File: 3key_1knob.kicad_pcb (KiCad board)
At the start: 2 copper layers, 99.2 x 35 mm, 18 parts, among them J1 Conn_01x02, SW1 RotaryEncoder_Switch, U4 Kailh_socket_MX, U5 Kailh_socket_MX, U6 Kailh_socket_MX

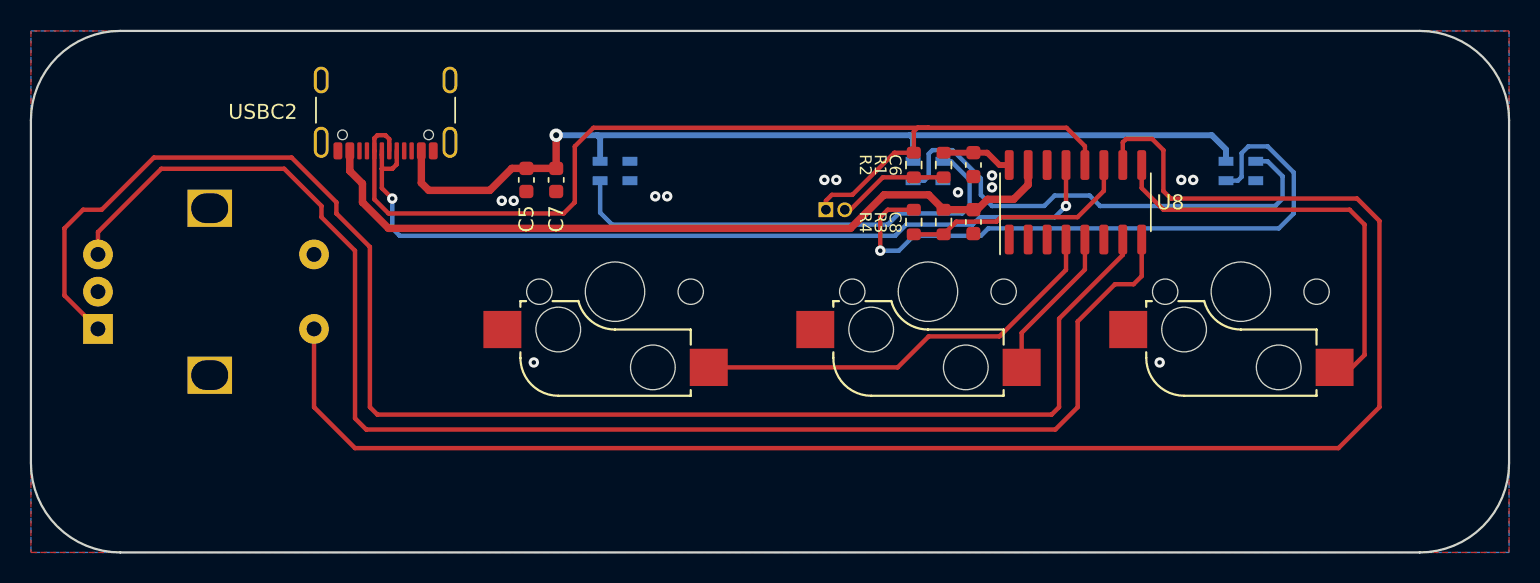
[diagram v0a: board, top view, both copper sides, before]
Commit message: Add mounting holes around corners
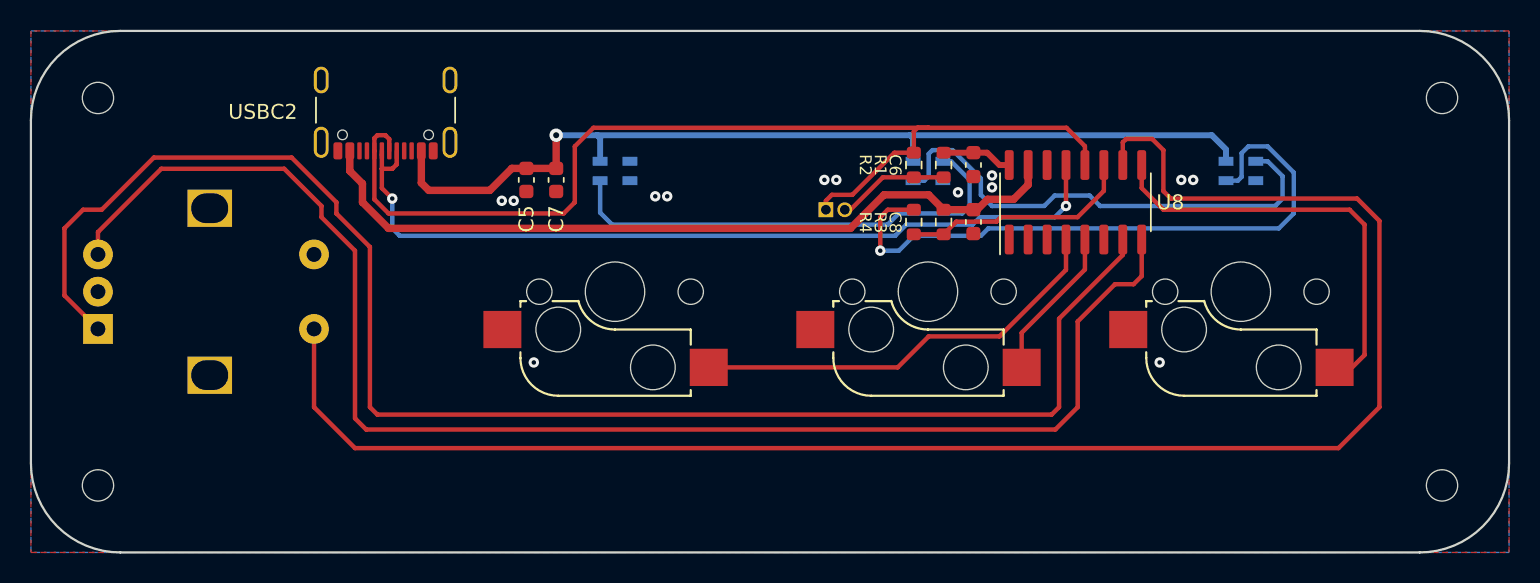
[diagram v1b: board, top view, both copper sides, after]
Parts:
- added REF**: MountingHole_2.1mm, MountingHole:MountingHole_2.1mm, F.Cu at (194.7, 130.5)
- added REF**: MountingHole_2.1mm, MountingHole:MountingHole_2.1mm, F.Cu at (194.7, 104.5)
- added REF**: MountingHole_2.1mm, MountingHole:MountingHole_2.1mm, F.Cu at (104.5, 104.5)
- added REF**: MountingHole_2.1mm, MountingHole:MountingHole_2.1mm, F.Cu at (104.5, 130.5)
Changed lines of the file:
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@@
     )
+  )
+  (footprint "MountingHole:MountingHole_2.1mm" (layer "F.Cu")
+    (at 194.7 130.5)
+    (descr "Mounting Hole 2.1mm, no annular")
+    (tags "mounting hole 2.1mm no annular")
+    (attr exclude_from_pos_files exclude_from_bom)
+    (fp_text reference "REF**" (at 0 -3.2) (layer "F.SilkS") hide
+        (effects (font (size 1 1) (thickness 0.15)))
+    )
+    (fp_text value "MountingHole_2.1mm" (at 0 3.2) (layer "F.Fab") hide
+        (effects (font (size 1 1) (thickness 0.15)))
+    )
+    (fp_text user "${REFERENCE}" (at 0 0) (layer "F.Fab") hide
+        (effects (font (size 1 1) (thickness 0.15)))
+    )
+    (fp_circle (center 0 0) (end 2.1 0)
+      (stroke (width 0.15) (type solid)) (fill none) (layer "Cmts.User"))
+    (fp_circle (center 0 0) (end 2.35 0)
+      (stroke (width 0.05) (type solid)) (fill none) (layer "F.CrtYd"))
+    (pad "" np_thru_hole circle (at 0 0) (size 2.1 2.1) (drill 2.1) (layers "F&B.Cu" "*.Mask"))
   )
   (footprint "Resistor_SMD:R_0603_1608Metric" (layer "F.Cu")
@@
     )
   )
+  (footprint "MountingHole:MountingHole_2.1mm" (layer "F.Cu")
+    (at 194.7 104.5)
+    (descr "Mounting Hole 2.1mm, no annular")
+    (tags "mounting hole 2.1mm no annular")
+    (attr exclude_from_pos_files exclude_from_bom)
+    (fp_text reference "REF**" (at 0 -3.2) (layer "F.SilkS") hide
+        (effects (font (size 1 1) (thickness 0.15)))
+    )
+    (fp_text value "MountingHole_2.1mm" (at 0 3.2) (layer "F.Fab") hide
+        (effects (font (size 1 1) (thickness 0.15)))
+    )
+    (fp_text user "${REFERENCE}" (at 0 0) (layer "F.Fab") hide
+        (effects (font (size 1 1) (thickness 0.15)))
+    )
+    (fp_circle (center 0 0) (end 2.1 0)
+      (stroke (width 0.15) (type solid)) (fill none) (layer "Cmts.User"))
+    (fp_circle (center 0 0) (end 2.35 0)
+      (stroke (width 0.05) (type solid)) (fill none) (layer "F.CrtYd"))
+    (pad "" np_thru_hole circle (at 0 0) (size 2.1 2.1) (drill 2.1) (layers "F&B.Cu" "*.Mask"))
+  )
   (footprint "Capacitor_SMD:C_0603_1608Metric" (layer "F.Cu")
     (at 163.25 112.825 -90)
@@
       (rotate (xyz 0 0 0))
     )
+  )
+  (footprint "MountingHole:MountingHole_2.1mm" (layer "F.Cu")
+    (at 104.5 104.5)
+    (descr "Mounting Hole 2.1mm, no annular")
+    (tags "mounting hole 2.1mm no annular")
+    (attr exclude_from_pos_files exclude_from_bom)
+    (fp_text reference "REF**" (at 0 -3.2) (layer "F.SilkS") hide
+        (effects (font (size 1 1) (thickness 0.15)))
+    )
+    (fp_text value "MountingHole_2.1mm" (at 0 3.2) (layer "F.Fab") hide
+        (effects (font (size 1 1) (thickness 0.15)))
+    )
+    (fp_text user "${REFERENCE}" (at 0 0) (layer "F.Fab") hide
+        (effects (font (size 1 1) (thickness 0.15)))
+    )
+    (fp_circle (center 0 0) (end 2.1 0)
+      (stroke (width 0.15) (type solid)) (fill none) (layer "Cmts.User"))
+    (fp_circle (center 0 0) (end 2.35 0)
+      (stroke (width 0.05) (type solid)) (fill none) (layer "F.CrtYd"))
+    (pad "" np_thru_hole circle (at 0 0) (size 2.1 2.1) (drill 2.1) (layers "*.Cu" "*.Mask"))
   )
   (footprint "Capacitor_SMD:C_0603_1608Metric" (layer "F.Cu")
@@
     )
   )
+  (footprint "MountingHole:MountingHole_2.1mm" (layer "F.Cu")
+    (at 104.5 130.5)
+    (descr "Mounting Hole 2.1mm, no annular")
+    (tags "mounting hole 2.1mm no annular")
+    (attr exclude_from_pos_files exclude_from_bom)
+    (fp_text reference "REF**" (at 0 -3.2) (layer "F.SilkS") hide
+        (effects (font (size 1 1) (thickness 0.15)))
+    )
+    (fp_text value "MountingHole_2.1mm" (at 0 3.2) (layer "F.Fab") hide
+        (effects (font (size 1 1) (thickness 0.15)))
+    )
+    (fp_text user "${REFERENCE}" (at 0 0) (layer "F.Fab") hide
+        (effects (font (size 1 1) (thickness 0.15)))
+    )
+    (fp_circle (center 0 0) (end 2.1 0)
+      (stroke (width 0.15) (type solid)) (fill none) (layer "Cmts.User"))
+    (fp_circle (center 0 0) (end 2.35 0)
+      (stroke (width 0.05) (type solid)) (fill none) (layer "F.CrtYd"))
+    (pad "" np_thru_hole circle (at 0 0) (size 2.1 2.1) (drill 2.1) (layers "F&B.Cu" "*.Mask"))
+  )
   (footprint "keyswitches:Kailh_socket_MX" (layer "B.Cu")

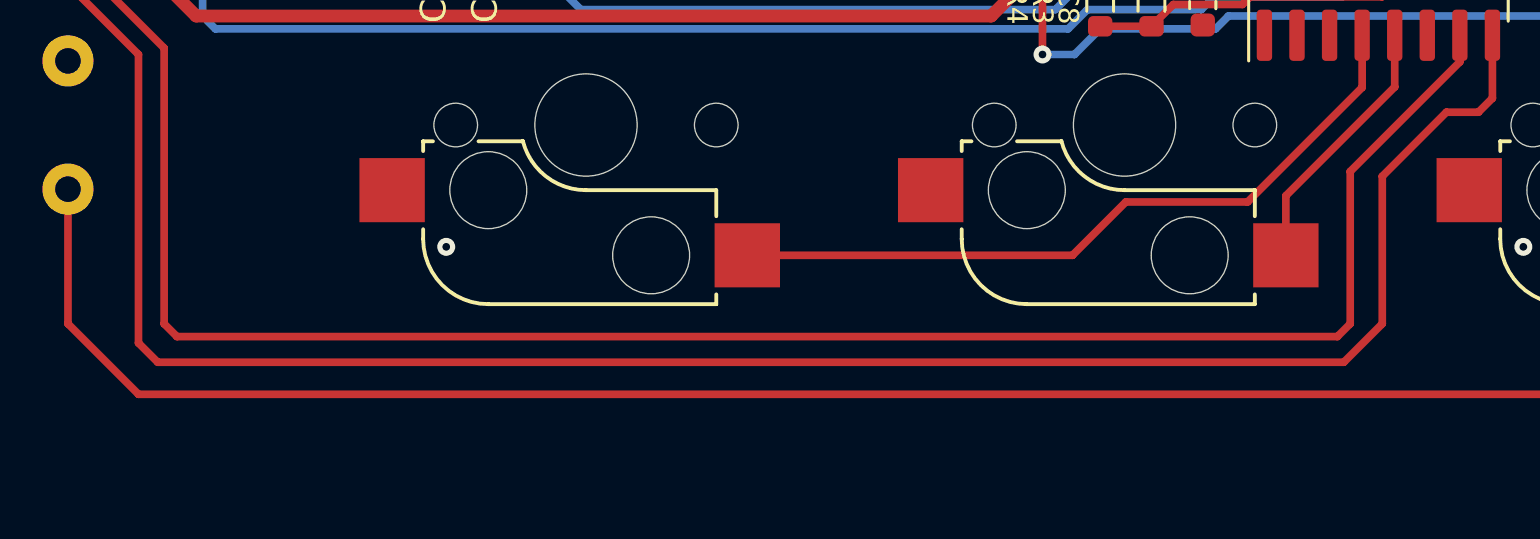
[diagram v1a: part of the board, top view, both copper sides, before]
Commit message: Convert signal nets to global nets; Update sch description; Minor PCB trace update
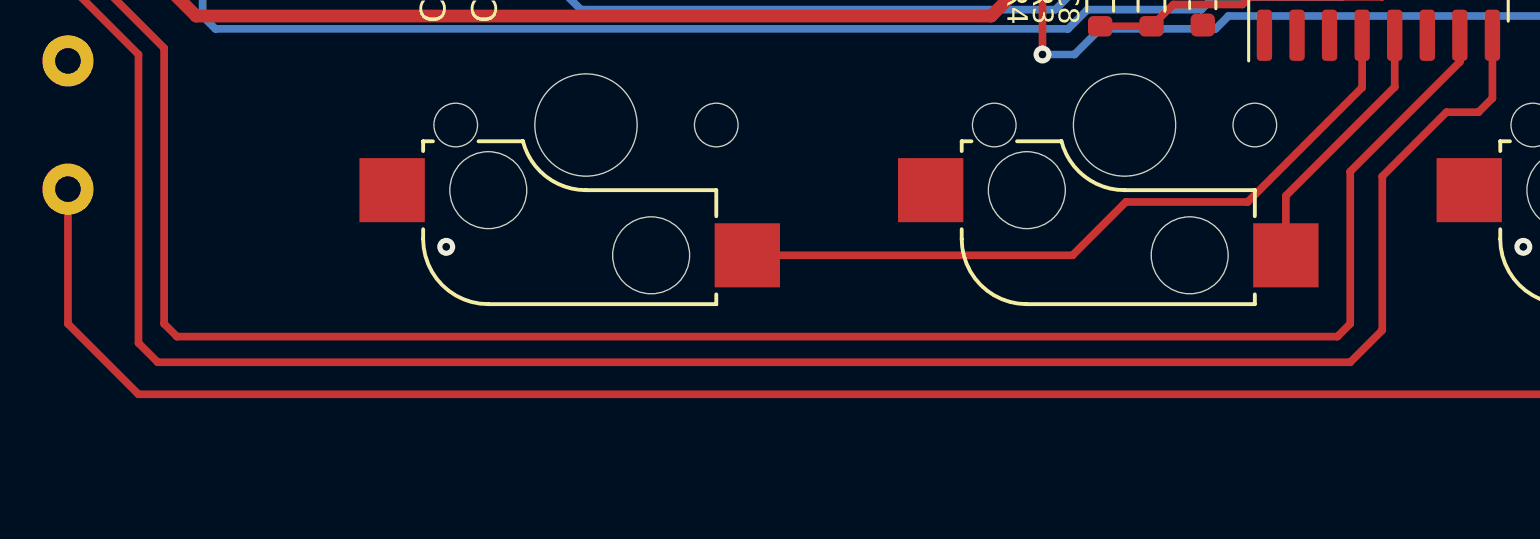
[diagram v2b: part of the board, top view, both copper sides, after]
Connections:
- net /CCW renamed CCW
- net /CW renamed CW
- net /D+ renamed D+
- net /D- renamed D-
- net /KEY1 renamed KEY1
- net /KEY2 renamed KEY2
- net /KEY3 renamed KEY3
- net /KEY4 renamed KEY4
- net /LED_DO renamed LED_DO
- SW1 pad MP: GND -> (no net)
